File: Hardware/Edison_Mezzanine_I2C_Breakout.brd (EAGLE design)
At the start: 30.5 x 44.5 mm, 21 parts, among them U2 PCA9306

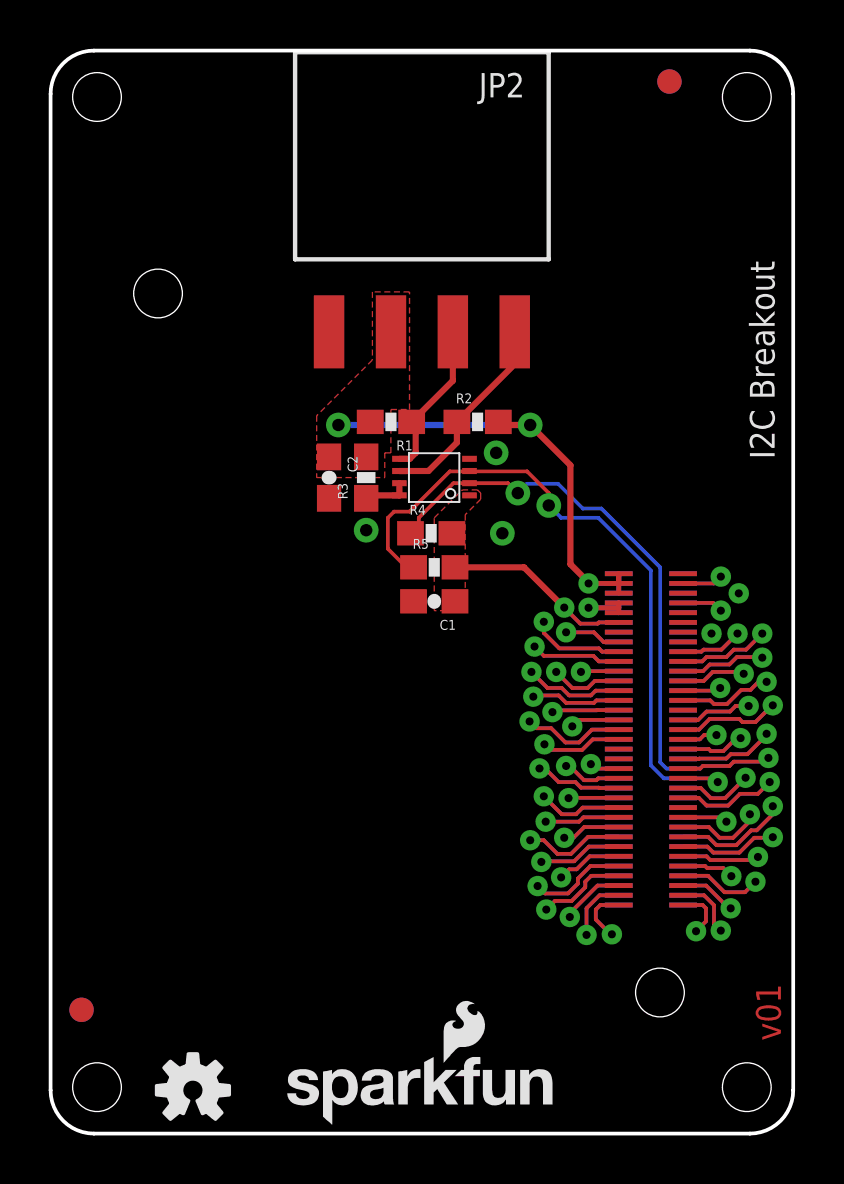
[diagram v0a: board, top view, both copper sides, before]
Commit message: corrected labels, added 3.3v regulator and corrected DCIN pin
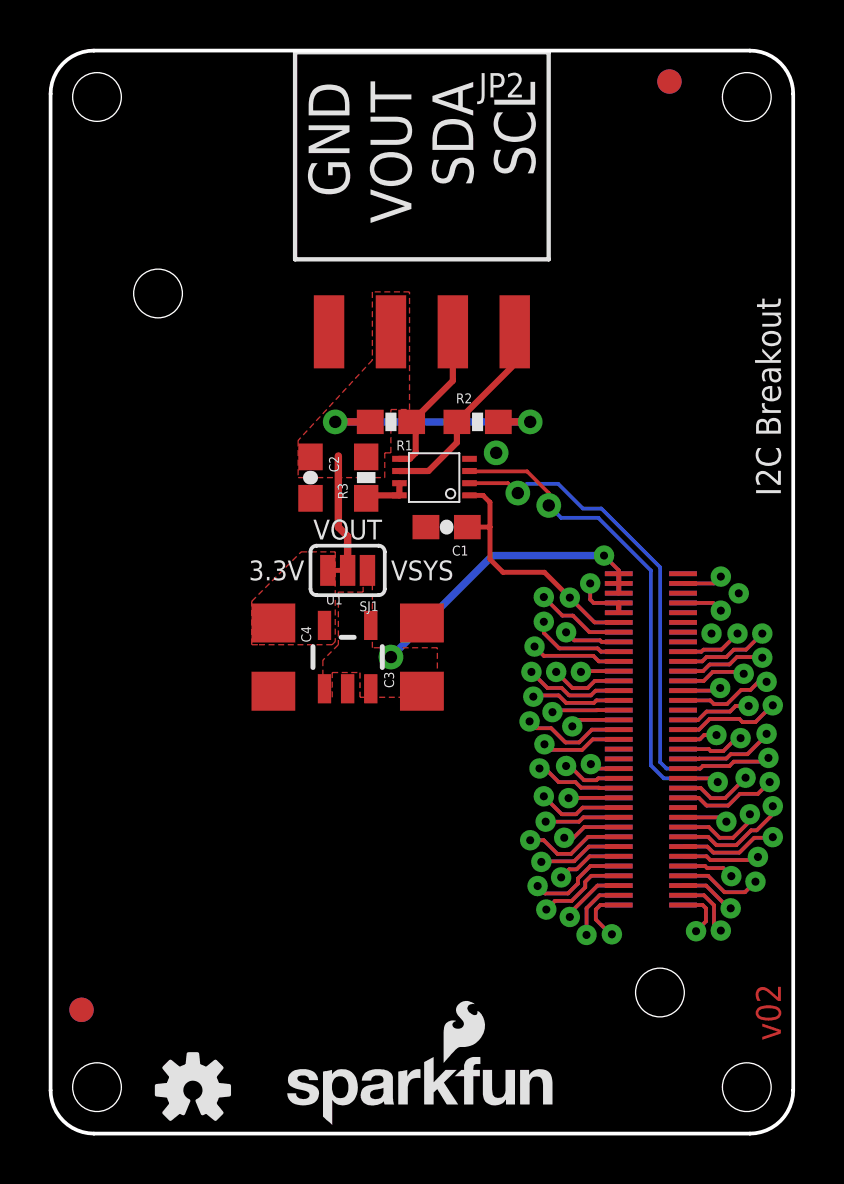
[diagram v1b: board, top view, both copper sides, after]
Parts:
- removed R4, R5: 2.2k, SparkFun-Resistors:0603-RES
- added C3, C4: 10uF, SparkFun-Capacitors:1206
- added SJ1: Power Select, SparkFun-Passives:PAD-JUMPER-3-2OF3_NC_BY_TRACE_YES_SILK_FULL_BOX
- added U1: (no value), SparkFun-PowerIC:SOT23-5
- moved C1 3.09 mm to (16.3, 24.9)
- moved C2 0.76 mm to (10.7, 26.9)
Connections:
- new net 3.3V-REGULATED: C4.1, SJ1.3, U1.5
- new net DCIN: U$2.14, U$3.14
- new net VOUT: C2.1, JP2.3, R1.2, R2.2, R3.2, SJ1.2
- net 1.8V: no longer R4.2, R5.2
- net GND: now also C3.2, C4.2, U1.2
- net GP19_I2C_1_SCL: no longer R4.1
- net GP20_I2C_1_SDA: no longer R5.1
- net VSYS: now also C3.1, SJ1.1, U1.1, U1.3; no longer C2.1, JP2.3, R1.2, R2.2, R3.2
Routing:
- net VOUT: track 0.00 -> 16.1 mm, vias 0 -> 2
- net DCIN: track 0.00 -> 7.35 mm, vias 0 -> 1
- net VSYS: track 21.4 -> 14.2 mm, vias 3 -> 2
- net GP20_I2C_1_SDA: track 28.7 -> 21.9 mm
- net GP19_I2C_1_SCL: track 29.4 -> 26.0 mm
- net 1.8V: track 10.2 -> 13.0 mm
- net 3.3V: track 3.68 -> 4.98 mm
- added copper zone on layer 1, net 3.3V-REGULATED
- added copper zone on layer 1, net VOUT
- removed copper zone on layer 1, net 1.8V
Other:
- board text added: "3.3V"
- board text added: "VOUT"
- board text added: "v02"
- board text removed: "Connectors Go Here"
- board text removed: "LED's and selector switches go here"
- board text removed: "Max Board Length"
- board text removed: "Nothing goes here... I mean it."
- board text removed: "v01"
